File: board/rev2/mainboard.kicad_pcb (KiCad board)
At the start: 4 copper layers, 164.8 x 71.1 mm, 160 parts, among them Q1 WSD40120DN56G, SW1 MS-22D28-G020, SW2 MS-22D28-G020, SW3 MS-22D28-G020, SW4 TS-1088-AR02016, SW5 MS-22D28-G020, U1 TPD6S300A, U10 74VHC161, U11 IS61LV256AL, U12 74AHCT595, U13 IS61LV256AL, U14 74AHCT595, U15 74HCT245, U16 74HCT245, U17 TS3USB30ERSWR, U18 TS3USB30ERSWR, U19 LD1117AG-33-AA3-A-R, U2 TPS62933, U3 TPS259472A, U4 LM5050-1, U5 SiC451, U6 STM32G071CBUx, U7 ESP32-C6-WROOM-1, U8 TLV74311, U9 RP2354B, Y1 ABM8-272-T3

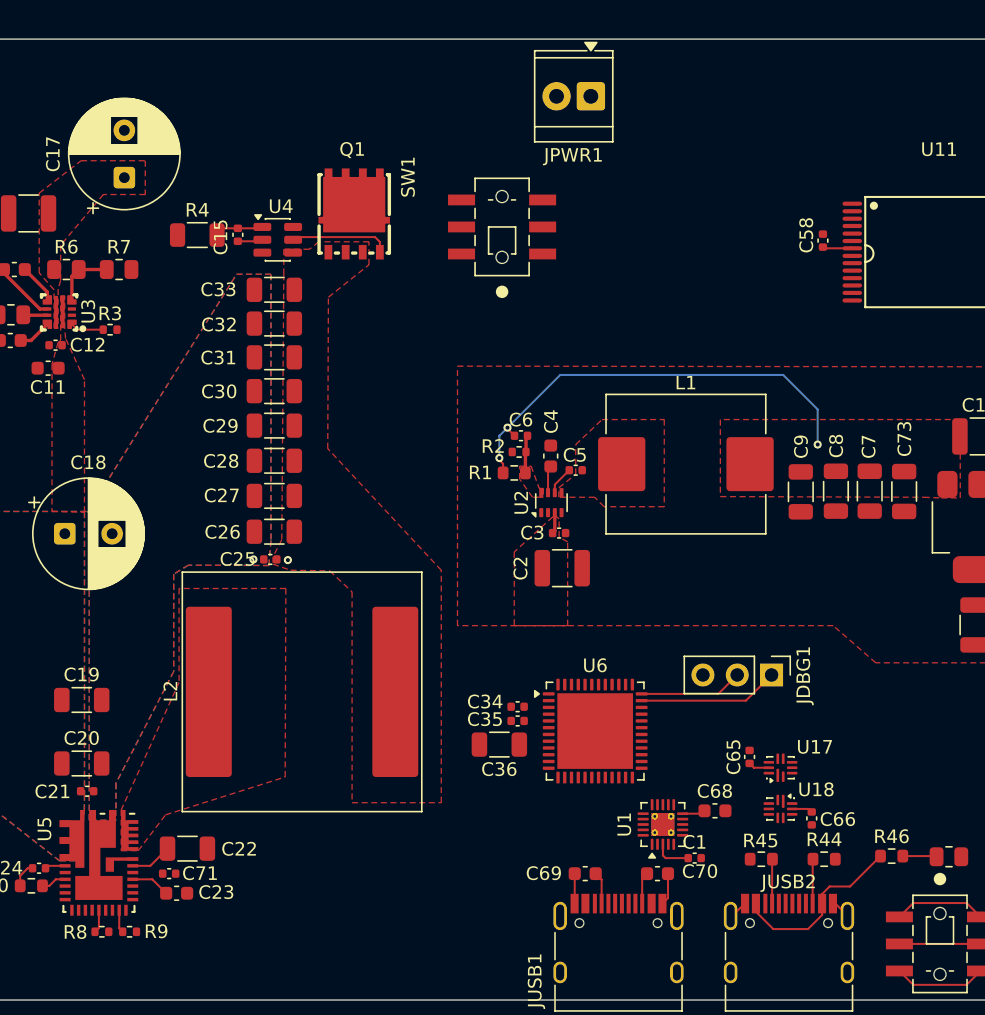
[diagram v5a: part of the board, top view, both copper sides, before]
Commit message: Route some more of the board: usb protection / mux
and some of the power mcu
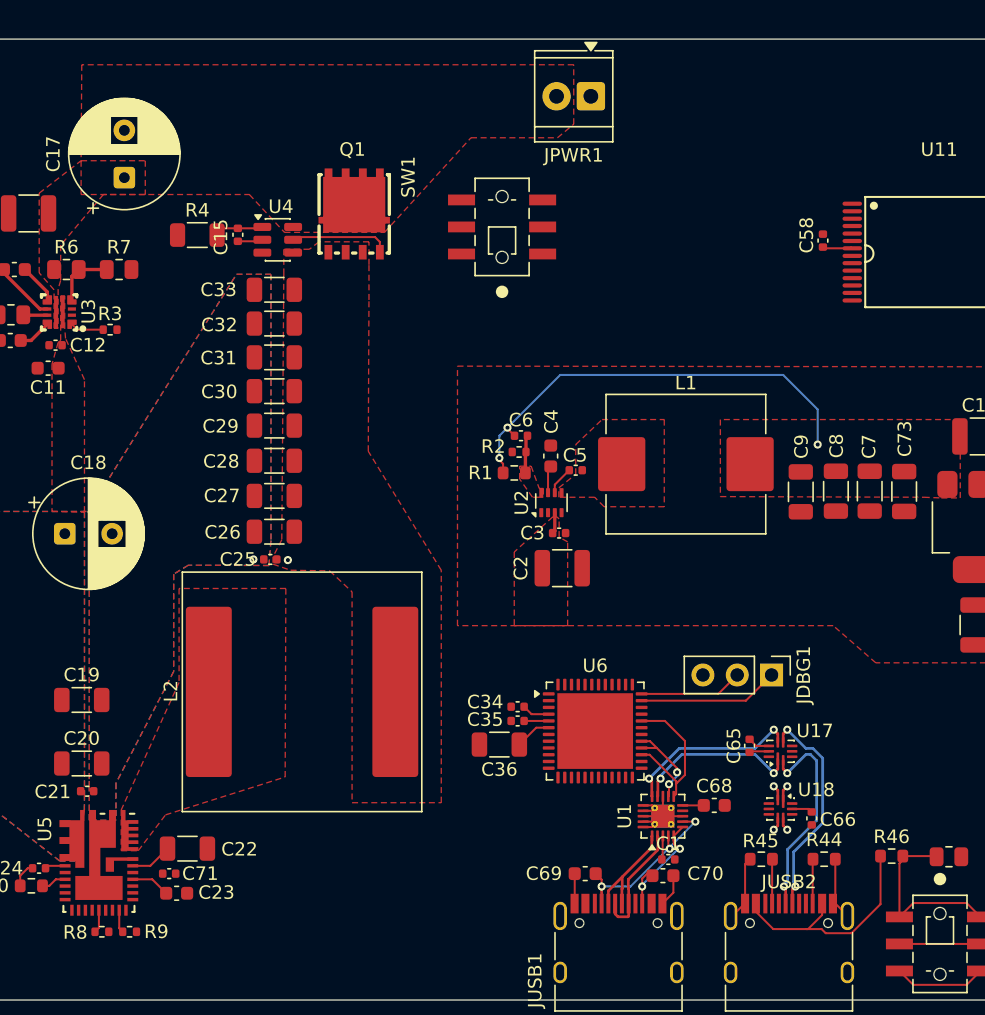
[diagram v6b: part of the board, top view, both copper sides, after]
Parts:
- moved C1 1.95 mm to (111.2, 150.8)
- moved U17 1.21 mm to (119.5, 142.8)
- moved C65 0.83 mm to (117.2, 142.4)
- moved U1 0.61 mm to (110.8, 147.6)
- moved C70 0.43 mm to (110.8, 152.0)
- moved C68 0.40 mm to (114.6, 146.8)
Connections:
- net Net-(U1-C_SBU1) renamed /Power/C_USB_D-
- net Net-(U1-C_SBU2) renamed /Power/C_USB_D+
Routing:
- net /Power/USB_D-: track 0.00 -> 28.1 mm, vias 0 -> 3
- net /Peripherals/AUX_USB_D-: track 0.00 -> 27.2 mm, vias 0 -> 3
- net /Power/USB_D+: track 0.00 -> 26.2 mm, vias 0 -> 3
- net /Peripherals/AUX_USB_D+: track 0.00 -> 25.5 mm, vias 0 -> 3
- net GND: track 22.9 -> 41.0 mm
- net /Power MCU/USB_CC2: track 0.00 -> 11.8 mm
- net Net-(JUSB1-CC1): track 2.40 -> 14.2 mm, vias 0 -> 3
- net /Power/C_USB_D+: track 0.00 -> 8.73 mm
- net /Power/C_USB_D-: track 0.00 -> 8.33 mm
- net /Power MCU/USB_CC1: track 0.00 -> 6.98 mm, vias 0 -> 2
- net Net-(JUSB1-CC2): track 2.36 -> 8.30 mm, vias 0 -> 2
- net VDD: track 36.8 -> 42.7 mm
- net Net-(R46-Pad2): track 9.79 -> 14.4 mm
- net /Peripherals/AUX_USB_VBUS: track 13.5 -> 17.4 mm
- net Net-(U1-VBIAS): track 2.78 -> 1.77 mm

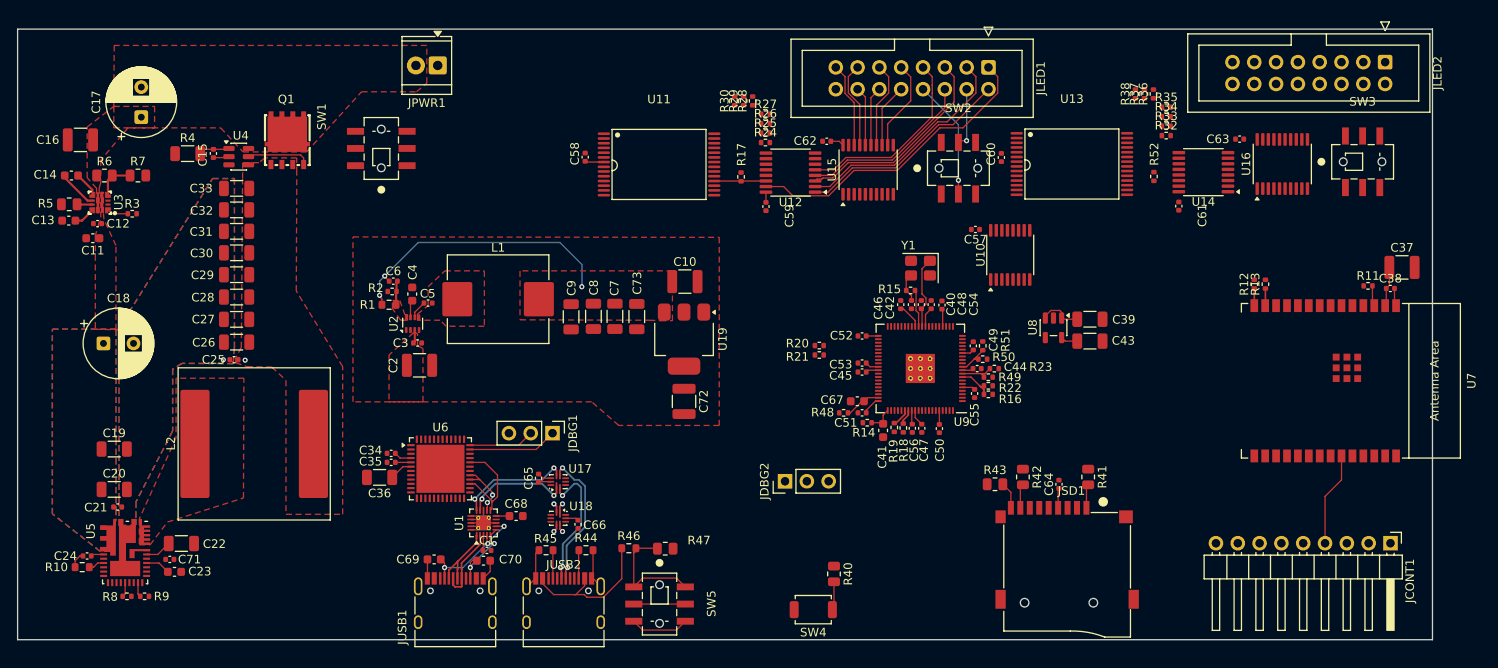
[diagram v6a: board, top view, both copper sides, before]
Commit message: Reorganize board, compress stuff closer to each other
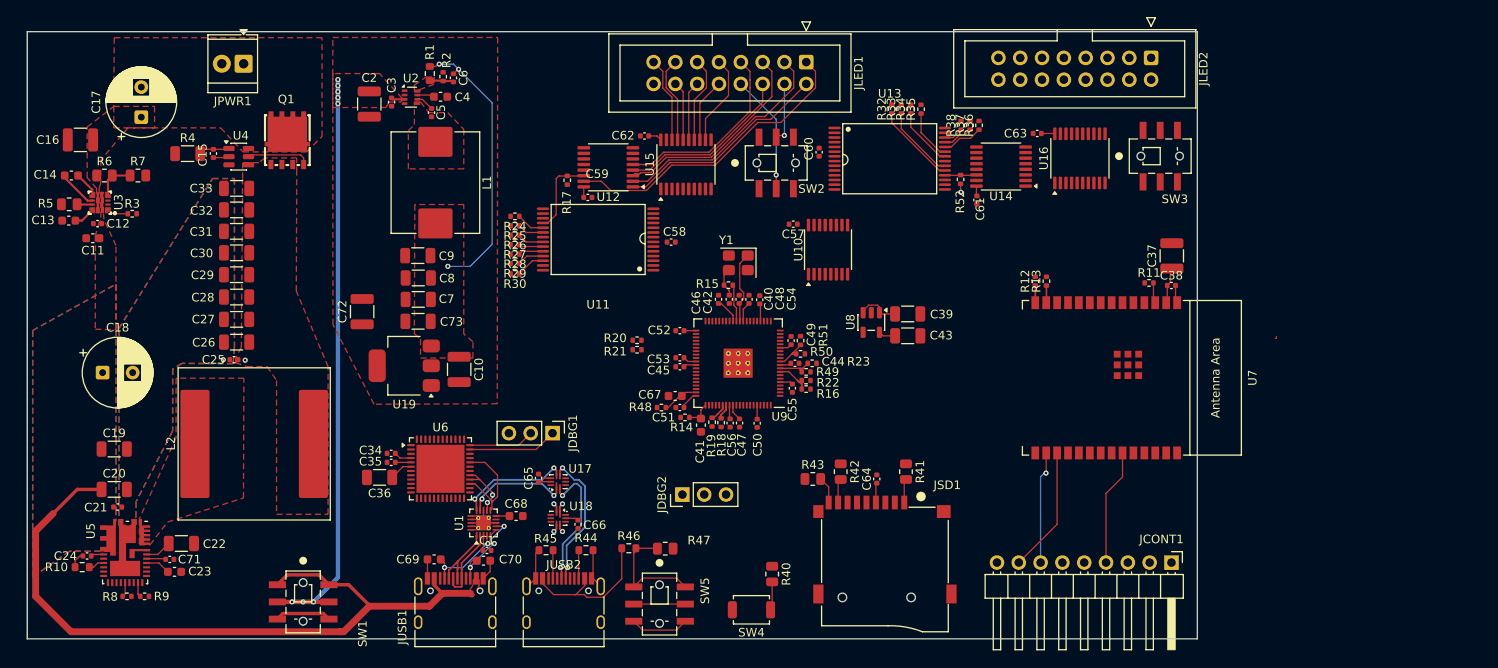
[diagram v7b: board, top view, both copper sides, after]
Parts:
- moved SW1 53.6 mm to (89.8, 156.8), turned to -90 degrees
- moved C72 38.9 mm to (96.7, 123.0), turned to 90 degrees
- moved R28 32.9 mm to (114.5, 116.3), turned to 180 degrees
- moved R27 32.9 mm to (114.5, 115.2), turned to 180 degrees
- moved U19 32.7 mm to (101.6, 129.3), turned to 180 degrees
- moved R29 32.7 mm to (114.5, 117.4), turned to 180 degrees
- moved R30 32.6 mm to (114.5, 118.6), turned to 180 degrees
- moved R32 32.1 mm to (158.3, 99.4), turned to 90 degrees
- moved R26 31.9 mm to (114.5, 114.1), turned to 180 degrees
- moved R25 31.1 mm to (114.5, 113.0), turned to 180 degrees
- moved C2 31.0 mm to (97.5, 98.8), turned to -90 degrees
- moved R33 30.9 mm to (159.4, 99.4), turned to 90 degrees
- moved R24 30.4 mm to (114.5, 111.9), turned to 180 degrees
- moved R34 29.8 mm to (160.6, 99.4), turned to 90 degrees
- moved R35 28.6 mm to (161.8, 99.4), turned to 90 degrees
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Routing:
- net /Power/VBUS: track 0.00 -> 88.7 mm
- net Net-(U2-VIN): track 1.58 -> 74.9 mm, vias 0 -> 8
- net /Peripherals/PWRBTN: track 0.00 -> 14.6 mm
- net /Peripherals/SELBTN: track 0.00 -> 13.2 mm, vias 0 -> 1
- net Net-(U13-I/O1): track 0.00 -> 9.58 mm
- net +5V: track 2.80 -> 12.1 mm
- net Net-(U13-I/O2): track 0.00 -> 8.64 mm
- net Net-(U13-I/O3): track 0.00 -> 6.98 mm
- net Net-(U13-I/O4): track 0.00 -> 5.92 mm
- net Net-(U13-I/O5): track 0.00 -> 4.80 mm
- net Net-(U13-I/O0): track 0.00 -> 3.69 mm
- net Net-(U13-I/O6): track 0.00 -> 3.52 mm
- net Net-(U11-I/O0): track 6.02 -> 9.48 mm
- net Net-(U11-I/O7): track 0.00 -> 3.38 mm
- net Net-(U11-I/O1): track 0.00 -> 3.30 mm
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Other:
- board size 164.8 x 71.1 mm -> 136.2 x 70.7 mm

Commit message: Finish board rev2
woo another pcb
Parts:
- removed R11: 20k, Resistor_SMD:R_0402_1005Metric
- added C74: 1uF, Capacitor_SMD:C_0603_1608Metric, F.Cu at (141.0, 154.4)
- added NT1: NetTie_2, NetTie:NetTie-2_SMD_Pad0.5mm, F.Cu at (82.8, 128.6)
- added NT2: NetTie_2, NetTie:NetTie-2_SMD_Pad0.5mm, F.Cu at (80.8, 128.6)
- added TP1: TestPoint, TestPoint:TestPoint_Pad_D1.0mm, F.Cu at (84.0, 158.3)
- added TP2: TestPoint, TestPoint:TestPoint_Pad_D1.0mm, F.Cu at (84.0, 153.3)
- added TP3: TestPoint, TestPoint:TestPoint_Pad_D1.0mm, F.Cu at (85.2, 127.5)
- added TP4: TestPoint, TestPoint:TestPoint_Pad_D1.0mm, F.Cu at (112.1, 123.2)
- added TP5: TestPoint, TestPoint:TestPoint_Pad_D1.0mm, F.Cu at (101.5, 123.5)
- added TP6: TestPoint, TestPoint:TestPoint_Pad_D1.0mm, F.Cu at (160.6, 137.2)
- added TP7: TestPoint, TestPoint:TestPoint_Pad_D1.0mm, F.Cu at (75.1, 127.1)
- C10, C16, C2, C37, C72: footprint Capacitor_SMD:C_1210_3225Metric -> Capacitor_SMD:C_1206_3216Metric
- JPWR1: footprint TerminalBlock_TE-Connectivity:TerminalBlock_TE_282834-2_1x02_P2.54mm_Horizontal -> Connector_KANGNEX:CONN-TH_4P-P9.50_WJHB9500M-9.5-04P-13-00A
- SW1, SW2, SW3, SW5: footprint Switch_Slide_SMD:SW-SMD_MS-22D28-G020 -> Switch_Slide_SMD:SW-SMD_MS-22D17AG2.5
- moved C33 19.1 mm to (89.3, 126.2), turned to 0 degrees
- moved R21 19.0 mm to (141.3, 113.3)
- moved JDBG2 17.8 mm to (121.7, 131.5)
- moved C32 14.6 mm to (89.3, 123.8), turned to 0 degrees
- moved C17 12.4 mm to (70.5, 112.7)
- moved C31 10.5 mm to (89.3, 121.2), turned to 0 degrees
- moved C16 10.3 mm to (63.9, 113.3)
- moved R4 10.2 mm to (76.2, 114.8)
- moved R7 9.98 mm to (70.5, 117.1)
- moved JPWR1 9.81 mm to (77.8, 102.5)
- moved C11 9.45 mm to (65.3, 123.9)
- moved C12 9.45 mm to (65.9, 122.2)
- moved C15 9.45 mm to (79.3, 114.0)
- moved R3 9.45 mm to (69.9, 121.0)
- moved R5 9.45 mm to (62.6, 120.0)
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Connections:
- net Net-(U2-VIN) renamed /Power/3VIN
- JPWR1 pad 1: GND -> +5V
- JSD1 pad 5: /Display MCU/CLK -> /Display MCU/SDCLK
- U11 pad 21: /Decoder/Output Stage A/PIX_CNT_Q2 -> /Decoder/MEM_A13
- U11 pad 24: /Decoder/Output Stage A/PIX_CNT_Q1 -> /Decoder/Output Stage A/PIX_CNT_Q2
- U11 pad 25: /Decoder/Output Stage A/PIX_CNT_Q0 -> /Decoder/Output Stage A/PIX_CNT_Q1
- U11 pad 26: /Decoder/MEM_A13 -> /Decoder/Output Stage A/PIX_CNT_Q0
- U13 pad 21: /Decoder/Output Stage A/PIX_CNT_Q2 -> /Decoder/MEM_A13
- U13 pad 24: /Decoder/Output Stage A/PIX_CNT_Q1 -> /Decoder/Output Stage A/PIX_CNT_Q2
- U13 pad 25: /Decoder/Output Stage A/PIX_CNT_Q0 -> /Decoder/Output Stage A/PIX_CNT_Q1
- U13 pad 26: /Decoder/MEM_A13 -> /Decoder/Output Stage A/PIX_CNT_Q0
- U5 pad 11: GND -> /Power/5V Reg/VSEN-
- U5 pad 12: /Power/5V_REG -> /Power/5V Reg/VSEN+
- U6 pad 39: /Power MCU/ESP_RESET -> unconnected-(U6-PD1-Pad39)
- U7 pad 3: /Power MCU/ESP_RESET -> RESET
- U9 pad 16: /Decoder/PIX_MEM_PA0 -> /Decoder/PIX_MEM_PB2
- U9 pad 17: /Decoder/PIX_MEM_PA1 -> /Decoder/PIX_MEM_PB1
- U9 pad 18: /Decoder/PIX_MEM_PA2 -> /Decoder/PIX_MEM_PB0
- U9 pad 19: /Decoder/PIX_MEM_PA3 -> /Decoder/PIX_MEM_PB3
- U9 pad 20: /Decoder/PIX_MEM_PA4 -> /Decoder/PIX_MEM_PB4
- U9 pad 21: /Decoder/PIX_MEM_PA5 -> /Decoder/PIX_MEM_PB5
- U9 pad 22: /Decoder/PIX_MEM_PA6 -> /Decoder/PIX_MEM_PB6
- U9 pad 23: /Decoder/PIX_MEM_PA7 -> /Decoder/PIX_MEM_PB7
- U9 pad 25: /Decoder/PIX_MEM_PB0 -> /Decoder/PIX_MEM_PA0
- U9 pad 26: /Decoder/PIX_MEM_PB1 -> /Decoder/PIX_MEM_PA1
- U9 pad 27: /Decoder/PIX_MEM_PB2 -> /Decoder/PIX_MEM_PA2
- U9 pad 28: /Decoder/PIX_MEM_PB3 -> /Decoder/PIX_MEM_PA3
- U9 pad 3: /Display MCU/CLK -> /Display MCU/SDCLK
- U9 pad 36: /Decoder/PIX_MEM_PB4 -> /Decoder/PIX_MEM_PA4
- U9 pad 37: /Decoder/PIX_MEM_PB5 -> /Decoder/PIX_MEM_PA5
- U9 pad 38: /Decoder/PIX_MEM_PB6 -> /Decoder/PIX_MEM_PA6
- U9 pad 39: /Decoder/PIX_MEM_PB7 -> /Decoder/PIX_MEM_PA7
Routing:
- net +5V: track 12.1 -> 235.4 mm, vias 0 -> 43
- net RESET: track 3.06 -> 185.8 mm, vias 0 -> 6
- net /Decoder/PANEL_RGB_OE: track 0.00 -> 119.2 mm, vias 0 -> 3
- net /Decoder/MEM_A13: track 0.00 -> 116.7 mm, vias 0 -> 2
- net /Power MCU/COMM1.TX: track 0.00 -> 92.8 mm, vias 0 -> 2
- net /Decoder/PIX_CLK: track 0.00 -> 80.7 mm, vias 0 -> 4
- net /Decoder/RGB_CLK: track 0.00 -> 80.5 mm, vias 0 -> 4
- net /Display MCU/PANEL_OE: track 0.00 -> 78.2 mm, vias 0 -> 3
- net /Display MCU/PANEL_LAT: track 0.00 -> 77.4 mm, vias 0 -> 3
- net /Display MCU/DET: track 3.13 -> 80.4 mm, vias 0 -> 2
- net /Display MCU/~{PIX_CLK}: track 0.00 -> 74.9 mm, vias 0 -> 3
- net /Display MCU/RMUX_E: track 0.00 -> 74.7 mm, vias 0 -> 3
- net /Decoder/MEM_IO: track 1.00 -> 75.4 mm, vias 1 -> 3
- net /Decoder/PIX_CNT_CE: track 0.00 -> 73.4 mm, vias 0 -> 2
- net /Decoder/PIX_CNT_PE: track 0.00 -> 73.1 mm, vias 0 -> 2
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- added copper zone on B.Cu, net +5V
- added copper zone on B.Cu, net /Power/5V_REG
- added copper zone on In1.Cu, net GND
- added copper zone on In2.Cu, net GND
- added copper zone on F.Cu, net Net-(U9-GPIO12)
- added copper zone on F.Cu, net VDD
- added copper zone on In2.Cu, net VDD
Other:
- board size 136.2 x 70.7 mm -> 136.2 x 71.1 mm
- board text added: "1.1V Reg"
- board text added: "3.3V Reg"
- board text added: "3VIN"
- board text added: "4.7V Switching Reg"
- board text added: "4V7"
- board text added: "5V / 20A Buck Regulator"
- board text added: "5V / GND"
- board text added: "5V Mux"
- board text added: "5V Passthru"
- board text added: "5V_REG"
- board text added: "DVDD"
- board text added: "Designed by Matthew Mirvish in Canada April 2026"
- board text added: "Display MCU"
- board text added: "GND"
- board text added: "GND SWCLK SWDIO"
- board text added: "MSign^{2} REV A"
- board text added: "Output Stage A"
- board text added: "Output Stage B"
- board text added: "PINOUT SEL"
- board text added: "PWR IN SEL"
- board text added: "Power MCU"
- board text added: "RESET"
- board text added: "SWDIO SWCLK GND"
- board text added: "USB SWAP"
- board text added: "USB-C"
- board text added: "VBUS"
- board text added: "VDD"
- board text added: "WiFi MCU"
- board text added: "aux"
- board text added: "main (power in)"
- board text added: "terminals (5V)"
